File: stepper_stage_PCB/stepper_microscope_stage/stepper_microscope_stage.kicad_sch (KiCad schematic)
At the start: 22 parts, among them J1 Conn_01x04_Socket

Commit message: Updated mounting holes to be M4 instead of M2
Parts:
- H1, H2, H3: footprint MountingHole:MountingHole_2.2mm_M2 -> MountingHole:MountingHole_4.3mm_M4; symbol Mechanical:MountingHole_Pad -> Mechanical:MountingHole
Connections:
- no-connect marks 19 -> 16
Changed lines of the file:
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@@
   (no_connect (at 167.64 107.95))
   (no_connect (at 142.24 97.79))
-  (no_connect (at 242.57 142.24))
-  (no_connect (at 242.57 118.11))
   (no_connect (at 160.02 87.63))
   (no_connect (at 167.64 130.81))
@@
   (no_connect (at 167.64 97.79))
   (no_connect (at 142.24 102.87))
-  (no_connect (at 242.57 130.81))
   (no_connect (at 157.48 87.63))
   (no_connect (at 142.24 113.03))
@@
     )
   )
-  (symbol (lib_id "Mechanical:MountingHole_Pad") (at 242.57 128.27 0) (unit 1)
+  (symbol (lib_id "Mechanical:MountingHole") (at 242.57 128.27 0) (unit 1)
     (in_bom yes) (on_board yes) (dnp no) (fields_autoplaced)
     (property "Reference" "H2" (at 245.11 125.73 0)
@@
       (effects (font (size 1.27 1.27)) (justify left))
     )
-    (property "Footprint" "MountingHole:MountingHole_2.2mm_M2" (at 242.57 128.27 0)
+    (property "Footprint" "MountingHole:MountingHole_4.3mm_M4" (at 242.57 128.27 0)
       (effects (font (size 1.27 1.27)) hide)
     )
@@
       (effects (font (size 1.27 1.27)) hide)
     )
-    (pin "1")
     (instances
       (project "stepper_microscope_stage"
@@
     )
   )
-  (symbol (lib_id "Mechanical:MountingHole_Pad") (at 242.57 115.57 0) (unit 1)
+  (symbol (lib_id "Mechanical:MountingHole") (at 242.57 115.57 0) (unit 1)
     (in_bom yes) (on_board yes) (dnp no) (fields_autoplaced)
     (property "Reference" "H1" (at 245.11 113.03 0)
@@
       (effects (font (size 1.27 1.27)) (justify left))
     )
-    (property "Footprint" "MountingHole:MountingHole_2.2mm_M2" (at 242.57 115.57 0)
+    (property "Footprint" "MountingHole:MountingHole_4.3mm_M4" (at 242.57 115.57 0)
       (effects (font (size 1.27 1.27)) hide)
     )
@@
       (effects (font (size 1.27 1.27)) hide)
     )
-    (pin "1")
     (instances
       (project "stepper_microscope_stage"
@@
     )
   )
-  (symbol (lib_id "Mechanical:MountingHole_Pad") (at 242.57 139.7 0) (unit 1)
+  (symbol (lib_id "Mechanical:MountingHole") (at 242.57 139.7 0) (unit 1)
     (in_bom yes) (on_board yes) (dnp no) (fields_autoplaced)
     (property "Reference" "H3" (at 245.11 137.16 0)
@@
       (effects (font (size 1.27 1.27)) (justify left))
     )
-    (property "Footprint" "MountingHole:MountingHole_2.2mm_M2" (at 242.57 139.7 0)
+    (property "Footprint" "MountingHole:MountingHole_4.3mm_M4" (at 242.57 139.7 0)
       (effects (font (size 1.27 1.27)) hide)
     )
@@
       (effects (font (size 1.27 1.27)) hide)
     )
-    (pin "1")
-    (instances
-      (project "stepper_microscope_stage"
+    (instances
+      (project "stepper_microscope_stage"

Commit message: Routed and filled board. Missing switch
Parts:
- added J2, J3: Screw_Terminal_01x04, TerminalBlock:TerminalBlock_Altech_AK300-4_P5.00mm, symbol Connector:Screw_Terminal_01x04
- added J4, J5: Conn_01x04_Socket, Connector_JST:JST_PH_B4B-PH-K_1x04_P2.00mm_Vertical, symbol Connector:Conn_01x04_Socket
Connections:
- new net: J2.1 (Pin_1), J4.4 (Pin_4)
- new net: J2.2 (Pin_2), J4.3 (Pin_3)
- new net: J2.3 (Pin_3), J4.2 (Pin_2)
- new net: J2.4 (Pin_4), J4.1 (Pin_1)
- new net: J3.4 (Pin_4), J5.1 (Pin_1)
- new net: J3.3 (Pin_3), J5.2 (Pin_2)
- new net: J3.2 (Pin_2), J5.3 (Pin_3)
- new net: J3.1 (Pin_1), J5.4 (Pin_4)
- no-connect marks 16 -> 17
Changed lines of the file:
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@@
   (no_connect (at 167.64 128.27))
   (no_connect (at 167.64 120.65))
+  (no_connect (at 209.55 86.36))
   (wire (pts (xy 189.23 48.26) (xy 186.69 48.26))
     (stroke (width 0) (type default))
@@
     (stroke (width 0) (type default))
   )
+  (wire (pts (xy 34.29 90.17) (xy 46.99 90.17))
+    (stroke (width 0) (type default))
+  )
   (wire (pts (xy 128.27 97.79) (xy 128.27 107.95))
     (stroke (width 0) (type default))
@@
     (stroke (width 0) (type default))
   )
+  (wire (pts (xy 34.29 116.84) (xy 46.99 116.84))
+    (stroke (width 0) (type default))
+  )
   (wire (pts (xy 186.69 48.26) (xy 186.69 52.07))
     (stroke (width 0) (type default))
@@
     (stroke (width 0) (type default))
   )
+  (wire (pts (xy 34.29 109.22) (xy 46.99 109.22))
+    (stroke (width 0) (type default))
+  )
+  (wire (pts (xy 34.29 111.76) (xy 46.99 111.76))
+    (stroke (width 0) (type default))
+  )
   (wire (pts (xy 64.77 54.61) (xy 64.77 59.69))
     (stroke (width 0) (type default))
@@
     (stroke (width 0) (type default))
   )
+  (wire (pts (xy 34.29 87.63) (xy 46.99 87.63))
+    (stroke (width 0) (type default))
+  )
   (wire (pts (xy 224.79 48.26) (xy 227.33 48.26))
     (stroke (width 0) (type default))
   )
+  (wire (pts (xy 34.29 114.3) (xy 46.99 114.3))
+    (stroke (width 0) (type default))
+  )
   (wire (pts (xy 96.52 40.64) (xy 105.41 40.64))
     (stroke (width 0) (type default))
@@
     (stroke (width 0) (type default))
   )
+  (wire (pts (xy 34.29 85.09) (xy 46.99 85.09))
+    (stroke (width 0) (type default))
+  )
   (wire (pts (xy 46.99 156.21) (xy 58.42 156.21))
     (stroke (width 0) (type default))
@@
   )
   (wire (pts (xy 152.4 138.43) (xy 152.4 149.86))
+    (stroke (width 0) (type default))
+  )
+  (wire (pts (xy 34.29 92.71) (xy 46.99 92.71))
     (stroke (width 0) (type default))
   )
@@
     )
   )
+  (symbol (lib_id "Connector:Screw_Terminal_01x04") (at 29.21 90.17 180) (unit 1)
+    (in_bom yes) (on_board yes) (dnp no) (fields_autoplaced)
+    (property "Reference" "J2" (at 29.21 78.74 0)
+      (effects (font (size 1.27 1.27)))
+    )
+    (property "Value" "Screw_Terminal_01x04" (at 29.21 81.28 0)
+      (effects (font (size 1.27 1.27)))
+    )
+    (property "Footprint" "TerminalBlock:TerminalBlock_Altech_AK300-4_P5.00mm" (at 29.21 90.17 0)
+      (effects (font (size 1.27 1.27)) hide)
+    )
+    (property "Datasheet" "~" (at 29.21 90.17 0)
+      (effects (font (size 1.27 1.27)) hide)
+    )
+    (pin "1")
+    (pin "2")
+    (pin "3")
+    (pin "4")
+    (instances
+      (project "stepper_microscope_stage"
+        (path "/994e4c91-1de9-4c0d-b1cb-8bdb391cfa47"
+          (reference "J2") (unit 1)
+        )
+      )
+    )
+  )
   (symbol (lib_id "power:GND") (at 132.08 59.69 0) (unit 1)
     (in_bom yes) (on_board yes) (dnp no) (fields_autoplaced)
@@
         (path "/994e4c91-1de9-4c0d-b1cb-8bdb391cfa47"
           (reference "STEPSIGGND1") (unit 1)
+        )
+      )
+    )
+  )
+  (symbol (lib_id "Connector:Conn_01x04_Socket") (at 52.07 111.76 0) (unit 1)
+    (in_bom yes) (on_board yes) (dnp no) (fields_autoplaced)
+    (property "Reference" "J5" (at 53.34 111.76 0)
+      (effects (font (size 1.27 1.27)) (justify left))
+    )
+    (property "Value" "Conn_01x04_Socket" (at 53.34 114.3 0)
+      (effects (font (size 1.27 1.27)) (justify left))
+    )
+    (property "Footprint" "Connector_JST:JST_PH_B4B-PH-K_1x04_P2.00mm_Vertical" (at 52.07 111.76 0)
+      (effects (font (size 1.27 1.27)) hide)
+    )
+    (property "Datasheet" "~" (at 52.07 111.76 0)
+      (effects (font (size 1.27 1.27)) hide)
+    )
+    (pin "1")
+    (pin "2")
+    (pin "3")
+    (pin "4")
+    (instances
+      (project "stepper_microscope_stage"
+        (path "/994e4c91-1de9-4c0d-b1cb-8bdb391cfa47"
+          (reference "J5") (unit 1)
         )
       )
@@
     )
   )
+  (symbol (lib_id "Connector:Screw_Terminal_01x04") (at 29.21 114.3 180) (unit 1)
+    (in_bom yes) (on_board yes) (dnp no) (fields_autoplaced)
+    (property "Reference" "J3" (at 29.21 102.87 0)
+      (effects (font (size 1.27 1.27)))
+    )
+    (property "Value" "Screw_Terminal_01x04" (at 29.21 105.41 0)
+      (effects (font (size 1.27 1.27)))
+    )
+    (property "Footprint" "TerminalBlock:TerminalBlock_Altech_AK300-4_P5.00mm" (at 29.21 114.3 0)
+      (effects (font (size 1.27 1.27)) hide)
+    )
+    (property "Datasheet" "~" (at 29.21 114.3 0)
+      (effects (font (size 1.27 1.27)) hide)
+    )
+    (pin "1")
+    (pin "2")
+    (pin "3")
+    (pin "4")
+    (instances
+      (project "stepper_microscope_stage"
+        (path "/994e4c91-1de9-4c0d-b1cb-8bdb391cfa47"
+          (reference "J3") (unit 1)
+        )
+      )
+    )
+  )
   (symbol (lib_id "power:GND") (at 251.46 55.88 0) (unit 1)
     (in_bom yes) (on_board yes) (dnp no) (fields_autoplaced)
@@
         )
       )
+    )
+  )
+  (symbol (lib_id "Connector:Conn_01x04_Socket") (at 52.07 87.63 0) (unit 1)
+    (in_bom yes) (on_board yes) (dnp no) (fields_autoplaced)
+    (property "Reference" "J4" (at 53.34 87.63 0)
+      (effects (font (size 1.27 1.27)) (justify left))
+    )
+    (property "Value" "Conn_01x04_Socket" (at 53.34 90.17 0)
+      (effects (font (size 1.27 1.27)) (justify left))
+    )
+    (property "Footprint" "Connector_JST:JST_PH_B4B-PH-K_1x04_P2.00mm_Vertical" (at 52.07 87.63 0)
+      (effects (font (size 1.27 1.27)) hide)
+    )
+    (property "Datasheet" "~" (at 52.07 87.63 0)
+      (effects (font (size 1.27 1.27)) hide)
+    )
+    (pin "1")
+    (pin "2")
+    (pin "3")
+    (pin "4")
+    (instances
+      (project "stepper_microscope_stage"
+        (path "/994e4c91-1de9-4c0d-b1cb-8bdb391cfa47"
+          (reference "J4") (unit 1)
+        )
+      )

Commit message: Version 1 acheived!
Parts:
- added SW1: SW_SPDT, Custom_switches:spdt_4mm_pitch_with_tension_relief, symbol Switch:SW_SPDT
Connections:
- net +24V: now also SW1.1 (A), SW1.2 (B)
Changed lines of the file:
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@@
   (no_connect (at 167.64 107.95))
   (no_connect (at 142.24 97.79))
+  (no_connect (at 201.93 82.55))
   (no_connect (at 160.02 87.63))
   (no_connect (at 167.64 130.81))
@@
   (no_connect (at 167.64 128.27))
   (no_connect (at 167.64 120.65))
-  (no_connect (at 209.55 86.36))
   (wire (pts (xy 189.23 48.26) (xy 186.69 48.26))
     (stroke (width 0) (type default))
@@
     (stroke (width 0) (type default))
   )
+  (wire (pts (xy 201.93 77.47) (xy 218.44 77.47))
+    (stroke (width 0) (type default))
+  )
   (wire (pts (xy 92.71 118.11) (xy 142.24 118.11))
     (stroke (width 0) (type default))
@@
   )
   (wire (pts (xy 186.69 52.07) (xy 186.69 55.88))
+    (stroke (width 0) (type default))
+  )
+  (wire (pts (xy 181.61 80.01) (xy 191.77 80.01))
     (stroke (width 0) (type default))
   )
@@
         (path "/994e4c91-1de9-4c0d-b1cb-8bdb391cfa47"
           (reference "#PWR05") (unit 1)
+        )
+      )
+    )
+  )
+  (symbol (lib_id "power:+24V") (at 181.61 80.01 90) (unit 1)
+    (in_bom yes) (on_board yes) (dnp no) (fields_autoplaced)
+    (property "Reference" "#PWR028" (at 185.42 80.01 0)
+      (effects (font (size 1.27 1.27)) hide)
+    )
+    (property "Value" "+24V" (at 177.8 80.01 90)
+      (effects (font (size 1.27 1.27)) (justify left))
+    )
+    (property "Footprint" "" (at 181.61 80.01 0)
+      (effects (font (size 1.27 1.27)) hide)
+    )
+    (property "Datasheet" "" (at 181.61 80.01 0)
+      (effects (font (size 1.27 1.27)) hide)
+    )
+    (pin "1")
+    (instances
+      (project "stepper_microscope_stage"
+        (path "/994e4c91-1de9-4c0d-b1cb-8bdb391cfa47"
+          (reference "#PWR028") (unit 1)
         )
       )
@@
         (path "/994e4c91-1de9-4c0d-b1cb-8bdb391cfa47"
           (reference "VIN1") (unit 1)
+        )
+      )
+    )
+  )
+  (symbol (lib_id "power:+24V") (at 218.44 77.47 270) (unit 1)
+    (in_bom yes) (on_board yes) (dnp no) (fields_autoplaced)
+    (property "Reference" "#PWR029" (at 214.63 77.47 0)
+      (effects (font (size 1.27 1.27)) hide)
+    )
+    (property "Value" "+24V" (at 222.25 77.47 90)
+      (effects (font (size 1.27 1.27)) (justify left))
+    )
+    (property "Footprint" "" (at 218.44 77.47 0)
+      (effects (font (size 1.27 1.27)) hide)
+    )
+    (property "Datasheet" "" (at 218.44 77.47 0)
+      (effects (font (size 1.27 1.27)) hide)
+    )
+    (pin "1")
+    (instances
+      (project "stepper_microscope_stage"
+        (path "/994e4c91-1de9-4c0d-b1cb-8bdb391cfa47"
+          (reference "#PWR029") (unit 1)
         )
       )
@@
         )
       )
+    )
+  )
+  (symbol (lib_id "Switch:SW_SPDT") (at 196.85 80.01 0) (unit 1)
+    (in_bom yes) (on_board yes) (dnp no) (fields_autoplaced)
+    (property "Reference" "SW1" (at 196.85 72.39 0)
+      (effects (font (size 1.27 1.27)))
+    )
+    (property "Value" "SW_SPDT" (at 196.85 74.93 0)
+      (effects (font (size 1.27 1.27)))
+    )
+    (property "Footprint" "Custom_switches:spdt_4mm_pitch_with_tension_relief" (at 196.85 80.01 0)
+      (effects (font (size 1.27 1.27)) hide)
+    )
+    (property "Datasheet" "~" (at 196.85 80.01 0)
+      (effects (font (size 1.27 1.27)) hide)
+    )
+    (pin "1")
+    (pin "2")
+    (pin "3")
+    (instances
+      (project "stepper_microscope_stage"
+        (path "/994e4c91-1de9-4c0d-b1cb-8bdb391cfa47"
+          (reference "SW1") (unit 1)
+        )
+      )

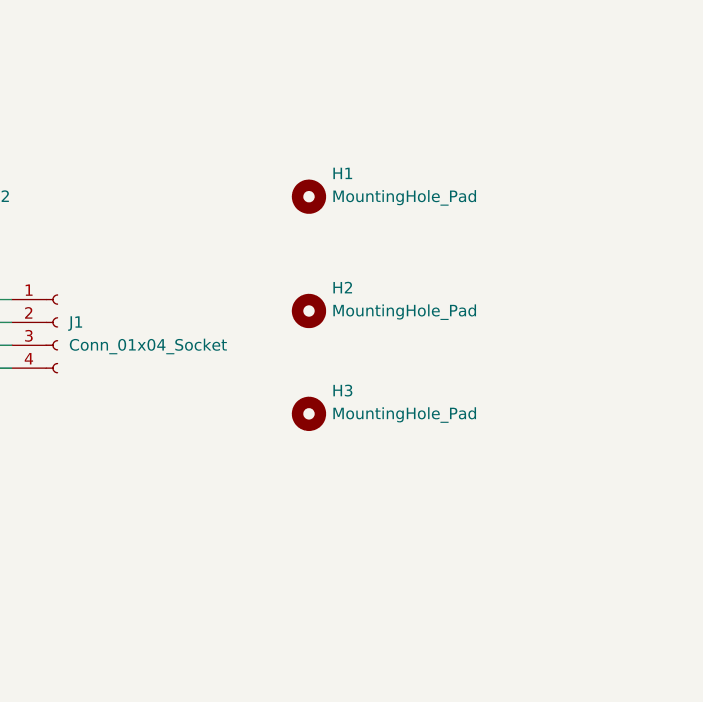
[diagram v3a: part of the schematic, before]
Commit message: Working. Must add following: (1) LCD space (2) ground plane
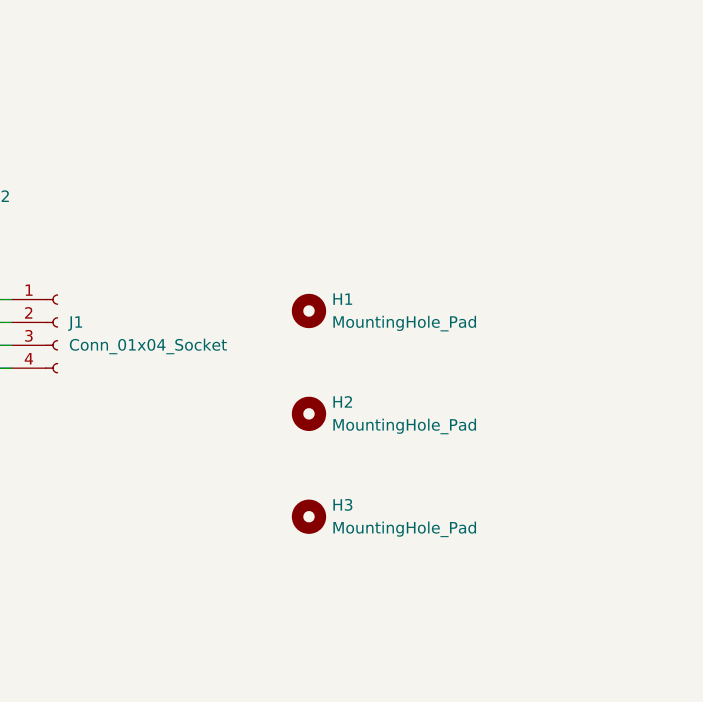
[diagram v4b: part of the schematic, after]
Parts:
- removed H1: MountingHole_Pad, MountingHole:MountingHole_4.3mm_M4, symbol Mechanical:MountingHole
- added H3: MountingHole_Pad, MountingHole:MountingHole_4.3mm_M4_Pad, symbol Mechanical:MountingHole
- H1: renamed from H2; footprint MountingHole:MountingHole_4.3mm_M4 -> MountingHole:MountingHole_4.3mm_M4_Pad
- H2: renamed from H3; footprint MountingHole:MountingHole_4.3mm_M4 -> MountingHole:MountingHole_4.3mm_M4_Pad
- J1: footprint Connector_PinSocket_2.00mm:PinSocket_1x04_P2.00mm_Vertical -> Connector_PinSocket_2.54mm:PinSocket_1x04_P2.54mm_Vertical
- J4, J5: footprint Connector_JST:JST_PH_B4B-PH-K_1x04_P2.00mm_Vertical -> Connector_JST:JST_EH_B4B-EH-A_1x04_P2.50mm_Vertical
- LIMIT1, LIMIT2: footprint Connector_JST:JST_PH_B3B-PH-K_1x03_P2.00mm_Vertical -> Connector_JST:JST_EH_B3B-EH-A_1x03_P2.50mm_Vertical
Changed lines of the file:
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@@
       (effects (font (size 1.27 1.27)))
     )
-    (property "Footprint" "Connector_JST:JST_PH_B3B-PH-K_1x03_P2.00mm_Vertical" (at 83.82 97.79 0)
+    (property "Footprint" "Connector_JST:JST_EH_B3B-EH-A_1x03_P2.50mm_Vertical" (at 83.82 97.79 0)
       (effects (font (size 1.27 1.27)) hide)
     )
@@
       (effects (font (size 1.27 1.27)))
     )
-    (property "Footprint" "Connector_JST:JST_PH_B3B-PH-K_1x03_P2.00mm_Vertical" (at 83.82 85.09 0)
+    (property "Footprint" "Connector_JST:JST_EH_B3B-EH-A_1x03_P2.50mm_Vertical" (at 83.82 85.09 0)
       (effects (font (size 1.27 1.27)) hide)
     )
@@
   (symbol (lib_id "Mechanical:MountingHole") (at 242.57 128.27 0) (unit 1)
     (in_bom yes) (on_board yes) (dnp no) (fields_autoplaced)
-    (property "Reference" "H2" (at 245.11 125.73 0)
-      (effects (font (size 1.27 1.27)) (justify left))
-    )
-    (property "Value" "MountingHole_Pad" (at 245.11 128.27 0)
-      (effects (font (size 1.27 1.27)) (justify left))
-    )
-    (property "Footprint" "MountingHole:MountingHole_4.3mm_M4" (at 242.57 128.27 0)
+    (property "Reference" "H1" (at 245.11 127 0)
+      (effects (font (size 1.27 1.27)) (justify left))
+    )
+    (property "Value" "MountingHole_Pad" (at 245.11 129.54 0)
+      (effects (font (size 1.27 1.27)) (justify left))
+    )
+    (property "Footprint" "MountingHole:MountingHole_4.3mm_M4_Pad" (at 242.57 128.27 0)
       (effects (font (size 1.27 1.27)) hide)
     )
@@
       (project "stepper_microscope_stage"
         (path "/994e4c91-1de9-4c0d-b1cb-8bdb391cfa47"
-          (reference "H2") (unit 1)
+          (reference "H1") (unit 1)
         )
       )
@@
       (effects (font (size 1.27 1.27)) (justify left))
     )
-    (property "Footprint" "Connector_PinSocket_2.00mm:PinSocket_1x04_P2.00mm_Vertical" (at 214.63 129.54 0)
+    (property "Footprint" "Connector_PinSocket_2.54mm:PinSocket_1x04_P2.54mm_Vertical" (at 214.63 129.54 0)
       (effects (font (size 1.27 1.27)) hide)
     )
@@
     )
   )
-  (symbol (lib_id "Mechanical:MountingHole") (at 242.57 115.57 0) (unit 1)
-    (in_bom yes) (on_board yes) (dnp no) (fields_autoplaced)
-    (property "Reference" "H1" (at 245.11 113.03 0)
-      (effects (font (size 1.27 1.27)) (justify left))
-    )
-    (property "Value" "MountingHole_Pad" (at 245.11 115.57 0)
-      (effects (font (size 1.27 1.27)) (justify left))
-    )
-    (property "Footprint" "MountingHole:MountingHole_4.3mm_M4" (at 242.57 115.57 0)
-      (effects (font (size 1.27 1.27)) hide)
-    )
-    (property "Datasheet" "~" (at 242.57 115.57 0)
-      (effects (font (size 1.27 1.27)) hide)
-    )
-    (instances
-      (project "stepper_microscope_stage"
-        (path "/994e4c91-1de9-4c0d-b1cb-8bdb391cfa47"
-          (reference "H1") (unit 1)
-        )
-      )
-    )
-  )
   (symbol (lib_id "power:PWR_FLAG") (at 45.72 48.26 180) (unit 1)
     (in_bom yes) (on_board yes) (dnp no) (fields_autoplaced)
@@
       (effects (font (size 1.27 1.27)) (justify left))
     )
-    (property "Footprint" "Connector_JST:JST_PH_B4B-PH-K_1x04_P2.00mm_Vertical" (at 52.07 111.76 0)
+    (property "Footprint" "Connector_JST:JST_EH_B4B-EH-A_1x04_P2.50mm_Vertical" (at 52.07 111.76 0)
       (effects (font (size 1.27 1.27)) hide)
     )
@@
     )
   )
+  (symbol (lib_id "Mechanical:MountingHole") (at 242.57 151.13 0) (unit 1)
+    (in_bom yes) (on_board yes) (dnp no) (fields_autoplaced)
+    (property "Reference" "H3" (at 245.11 149.86 0)
+      (effects (font (size 1.27 1.27)) (justify left))
+    )
+    (property "Value" "MountingHole_Pad" (at 245.11 152.4 0)
+      (effects (font (size 1.27 1.27)) (justify left))
+    )
+    (property "Footprint" "MountingHole:MountingHole_4.3mm_M4_Pad" (at 242.57 151.13 0)
+      (effects (font (size 1.27 1.27)) hide)
+    )
+    (property "Datasheet" "~" (at 242.57 151.13 0)
+      (effects (font (size 1.27 1.27)) hide)
+    )
+    (instances
+      (project "stepper_microscope_stage"
+        (path "/994e4c91-1de9-4c0d-b1cb-8bdb391cfa47"
+          (reference "H3") (unit 1)
+        )
+      )
+    )
+  )
   (symbol (lib_id "Connector:Screw_Terminal_01x03") (at 41.91 171.45 180) (unit 1)
     (in_bom yes) (on_board yes) (dnp no) (fields_autoplaced)
@@
       (effects (font (size 1.27 1.27)) (justify left))
     )
-    (property "Footprint" "Connector_JST:JST_PH_B4B-PH-K_1x04_P2.00mm_Vertical" (at 52.07 87.63 0)
+    (property "Footprint" "Connector_JST:JST_EH_B4B-EH-A_1x04_P2.50mm_Vertical" (at 52.07 87.63 0)
       (effects (font (size 1.27 1.27)) hide)
     )
@@
   (symbol (lib_id "Mechanical:MountingHole") (at 242.57 139.7 0) (unit 1)
     (in_bom yes) (on_board yes) (dnp no) (fields_autoplaced)
-    (property "Reference" "H3" (at 245.11 137.16 0)
-      (effects (font (size 1.27 1.27)) (justify left))
-    )
-    (property "Value" "MountingHole_Pad" (at 245.11 139.7 0)
-      (effects (font (size 1.27 1.27)) (justify left))
-    )
-    (property "Footprint" "MountingHole:MountingHole_4.3mm_M4" (at 242.57 139.7 0)
+    (property "Reference" "H2" (at 245.11 138.43 0)
+      (effects (font (size 1.27 1.27)) (justify left))
+    )
+    (property "Value" "MountingHole_Pad" (at 245.11 140.97 0)
+      (effects (font (size 1.27 1.27)) (justify left))
+    )
+    (property "Footprint" "MountingHole:MountingHole_4.3mm_M4_Pad" (at 242.57 139.7 0)
       (effects (font (size 1.27 1.27)) hide)
     )
@@
       (project "stepper_microscope_stage"
         (path "/994e4c91-1de9-4c0d-b1cb-8bdb391cfa47"
-          (reference "H3") (unit 1)
-        )
-      )
+          (reference "H2") (unit 1)
+        )
+      )
